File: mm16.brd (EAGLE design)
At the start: 100 x 80 mm, 57 parts, among them IC101 ATMEGA32-PU, IC102 DS1337, IC103 MAX483CPA, IC201 LTV847, IC202 LTV847, IC203 LTV847, IC204 LTV847, Q1 32,768kHz

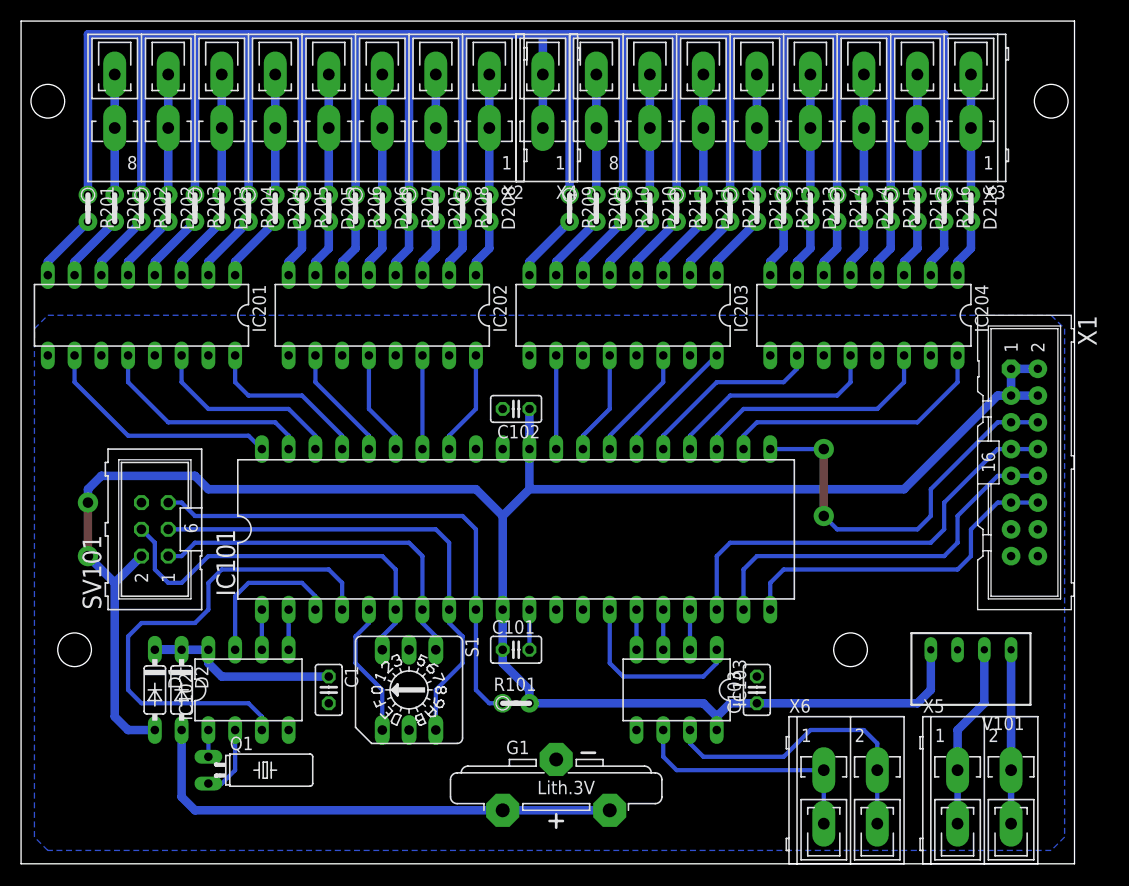
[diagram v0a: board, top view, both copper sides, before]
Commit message: Anschlussklemmen ausgetauscht
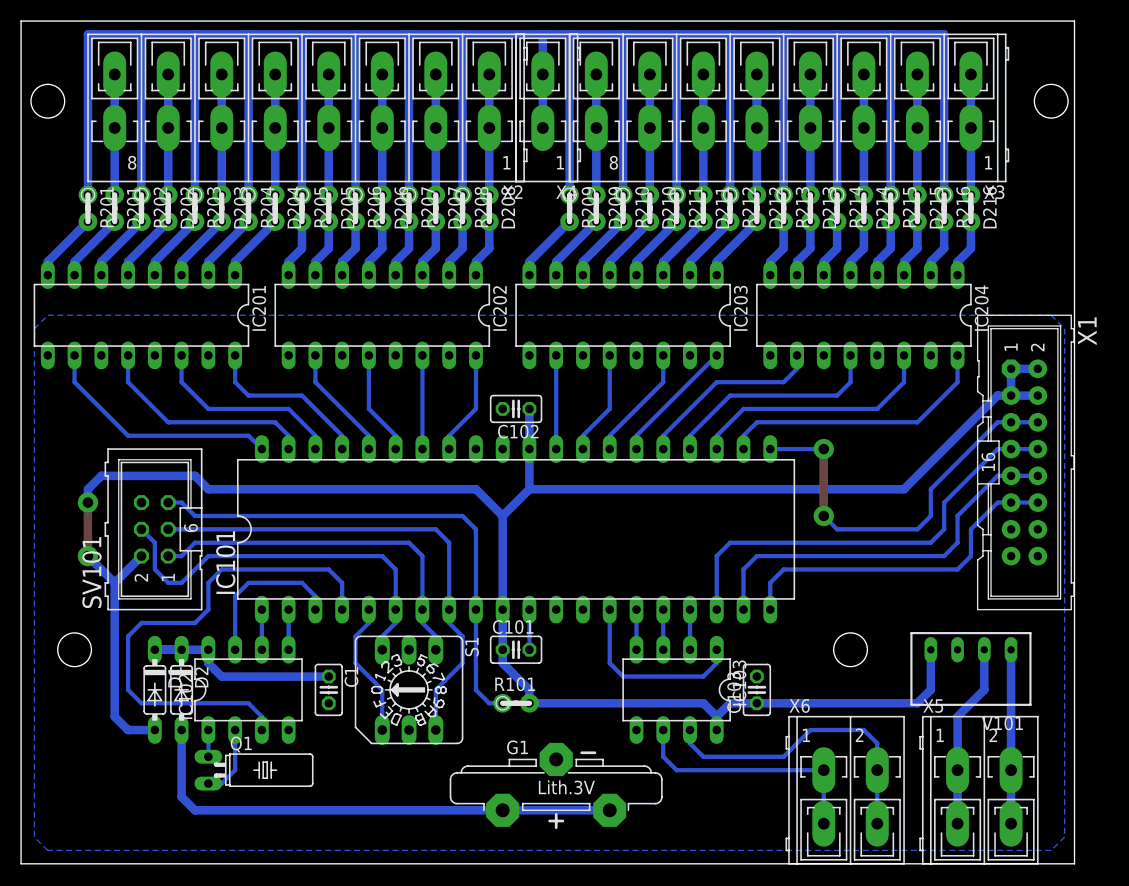
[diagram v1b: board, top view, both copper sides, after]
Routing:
- net N$83: track 11.4 -> 16.5 mm

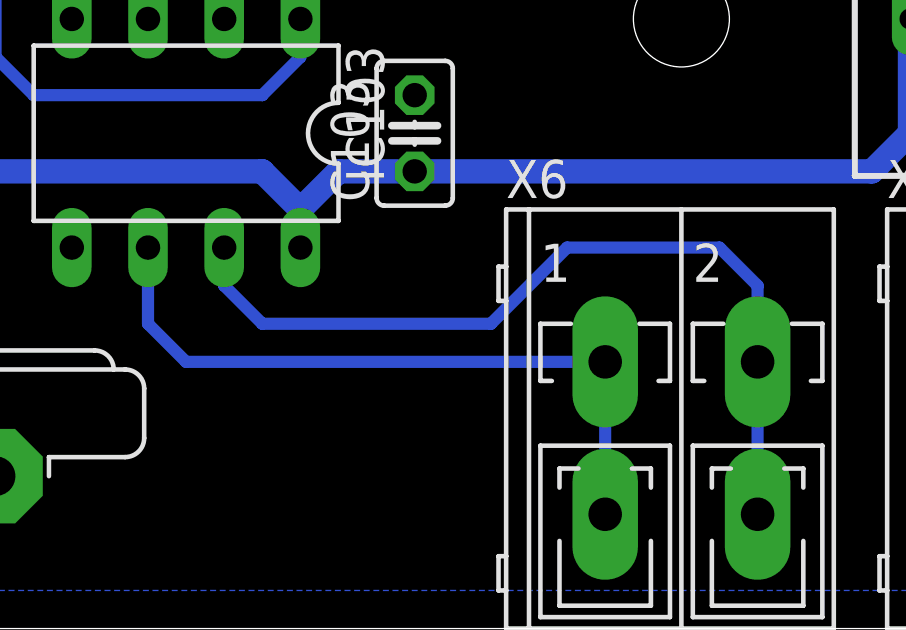
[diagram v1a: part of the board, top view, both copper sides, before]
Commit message: Optionaler Abschlusswiderstand eingefügt
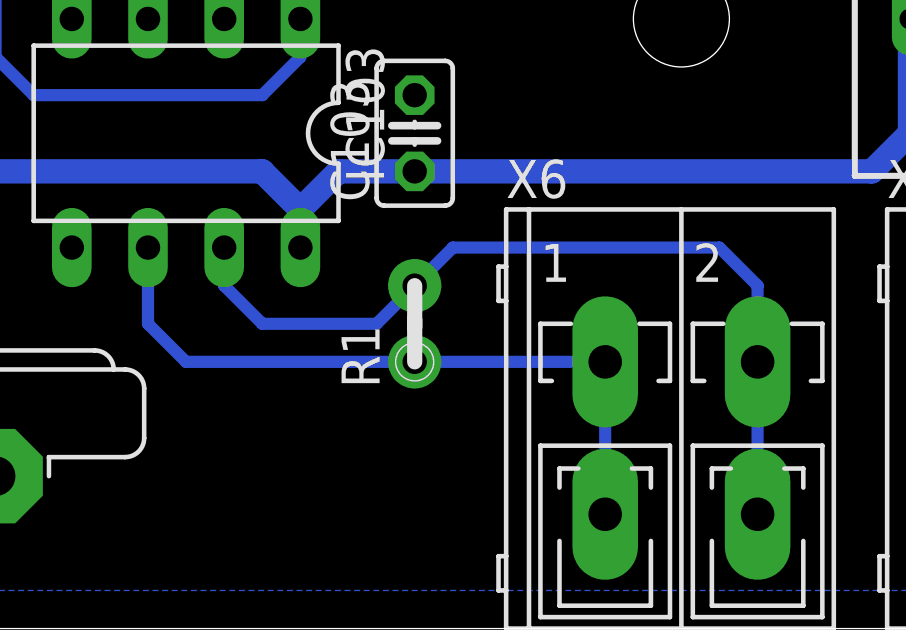
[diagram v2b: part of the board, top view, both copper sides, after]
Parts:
- added R1: 120Ω, passiv:0204V
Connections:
- removed net N$19: IC103.7, X6.A2, X6.B2
- new net N$22: IC103.7, R1.2, X6.A2, X6.B2
- net N$20: now also R1.1
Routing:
- net N$19: track 28.8 -> 0.00 mm
- net N$22: track 0.00 -> 28.8 mm
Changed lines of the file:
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@@
 <element name="X2" library="anschluss" package="WAGO_236-408" value="" x="26.67" y="71.12" rot="R180"/>
 <element name="X3" library="anschluss" package="WAGO_236-408" value="" x="72.39" y="71.12" rot="R180"/>
+<element name="R1" library="passiv" package="0204V" value="120Ω" x="69.85" y="10.16" rot="R90"/>
 </elements>
 <signals>
@@
 <wire x1="49.53" y1="74.93" x2="49.53" y2="78.74" width="0.8128" layer="16"/>
 </signal>
-<signal name="N$19">
-<contactref element="IC103" pad="7"/>
-<wire x1="63.5" y1="12.7" x2="63.5" y2="11.43" width="0.4064" layer="16"/>
-<wire x1="63.5" y1="11.43" x2="64.77" y2="10.16" width="0.4064" layer="16"/>
-<wire x1="64.77" y1="10.16" x2="72.39" y2="10.16" width="0.4064" layer="16"/>
-<wire x1="72.39" y1="10.16" x2="74.93" y2="12.7" width="0.4064" layer="16"/>
-<wire x1="74.93" y1="12.7" x2="80.01" y2="12.7" width="0.4064" layer="16"/>
-<wire x1="80.01" y1="12.7" x2="81.28" y2="11.43" width="0.4064" layer="16"/>
-<contactref element="X6" pad="B2" route="any" routetag="A"/>
-<contactref element="X6" pad="A2" route="any" routetag="A"/>
-<wire x1="81.28" y1="8.89" x2="81.28" y2="11.43" width="0.4064" layer="16"/>
-<wire x1="81.28" y1="8.89" x2="81.28" y2="3.81" width="0.4064" layer="16"/>
-</signal>
 <signal name="N$20">
 <contactref element="IC103" pad="6"/>
+<contactref element="X6" pad="A1" route="any" routetag="A"/>
+<contactref element="X6" pad="B1" route="any" routetag="A"/>
+<wire x1="76.2" y1="8.89" x2="76.2" y2="3.81" width="0.4064" layer="16"/>
+<contactref element="R1" pad="1"/>
 <wire x1="60.96" y1="12.7" x2="60.96" y2="10.16" width="0.4064" layer="16"/>
 <wire x1="60.96" y1="10.16" x2="62.23" y2="8.89" width="0.4064" layer="16"/>
-<contactref element="X6" pad="A1" route="any" routetag="A"/>
-<contactref element="X6" pad="B1" route="any" routetag="A"/>
-<wire x1="76.2" y1="8.89" x2="62.23" y2="8.89" width="0.4064" layer="16"/>
-<wire x1="76.2" y1="8.89" x2="76.2" y2="3.81" width="0.4064" layer="16"/>
+<wire x1="62.23" y1="8.89" x2="69.85" y2="8.89" width="0.4064" layer="16"/>
+<wire x1="69.85" y1="8.89" x2="76.2" y2="8.89" width="0.4064" layer="16"/>
 </signal>
 <signal name="VCC">
@@
 <wire x1="93.98" y1="8.89" x2="93.98" y2="3.81" width="0.8128" layer="16"/>
 </signal>
+<signal name="N$22">
+<contactref element="R1" pad="2"/>
+<contactref element="IC103" pad="7"/>
+<contactref element="X6" pad="B2" route="any" routetag="A"/>
+<contactref element="X6" pad="A2" route="any" routetag="A"/>
+<wire x1="63.5" y1="12.7" x2="63.5" y2="11.43" width="0.4064" layer="16"/>
+<wire x1="63.5" y1="11.43" x2="64.77" y2="10.16" width="0.4064" layer="16"/>
+<wire x1="80.01" y1="12.7" x2="81.28" y2="11.43" width="0.4064" layer="16"/>
+<wire x1="81.28" y1="8.89" x2="81.28" y2="11.43" width="0.4064" layer="16"/>
+<wire x1="81.28" y1="8.89" x2="81.28" y2="3.81" width="0.4064" layer="16"/>
+<wire x1="64.77" y1="10.16" x2="68.58" y2="10.16" width="0.4064" layer="16"/>
+<wire x1="68.58" y1="10.16" x2="69.85" y2="11.43" width="0.4064" layer="16"/>
+<wire x1="69.85" y1="11.43" x2="71.12" y2="12.7" width="0.4064" layer="16"/>
+<wire x1="71.12" y1="12.7" x2="80.01" y2="12.7" width="0.4064" layer="16"/>
+</signal>
 </signals>

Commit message: Batteriehalter ausgetauscht
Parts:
- G1: value CR2032V -> KZH20PCB-V; device battery:CR2032V -> batterie:KZH20PCB-V
- moved G1 1.80 mm to (49.5, 6.35), turned to 180 degrees
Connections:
- net N$21: now also G1.+1, G1.+2; no longer G1.+, G1.+@1
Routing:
- net N$21: track 47.5 -> 36.1 mm
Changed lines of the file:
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@@
 </classes>
 <designrules>
-<description language="de">&lt;b&gt;EAGLE Design Rules&lt;/b&gt;
-&lt;p&gt;
-Die Standard-Design-Rules sind so gewählt, dass sie für
-die meisten Anwendungen passen. Sollte ihre Platine
-besondere Anforderungen haben, treffen Sie die erforderlichen
-Einstellungen hier und speichern die Design Rules unter
-einem neuen Namen ab.</description>
-<description language="en">&lt;b&gt;EAGLE Design Rules&lt;/b&gt;
+<description language="de">
+&lt;b&gt;Standardwerte für Eigenbau&lt;/b&gt;
+</description>
+<description language="en">
+&lt;b&gt;EAGLE Design Rules&lt;/b&gt;
 &lt;p&gt;
 The default Design Rules have been set to cover
@@
 <param name="mtCopper" value="0.035mm 0.035mm 0.035mm 0.035mm 0.035mm 0.035mm 0.035mm 0.035mm 0.035mm 0.035mm 0.035mm 0.035mm 0.035mm 0.035mm 0.035mm 0.035mm"/>
 <param name="mtIsolate" value="1.5mm 0.15mm 0.2mm 0.15mm 0.2mm 0.15mm 0.2mm 0.15mm 0.2mm 0.15mm 0.2mm 0.15mm 0.2mm 0.15mm 0.2mm"/>
-<param name="mdWireWire" value="8mil"/>
-<param name="mdWirePad" value="8mil"/>
-<param name="mdWireVia" value="8mil"/>
-<param name="mdPadPad" value="8mil"/>
-<param name="mdPadVia" value="8mil"/>
-<param name="mdViaVia" value="8mil"/>
-<param name="mdSmdPad" value="8mil"/>
-<param name="mdSmdVia" value="8mil"/>
-<param name="mdSmdSmd" value="8mil"/>
+<param name="mdWireWire" value="16mil"/>
+<param name="mdWirePad" value="16mil"/>
+<param name="mdWireVia" value="16mil"/>
+<param name="mdPadPad" value="16mil"/>
+<param name="mdPadVia" value="16mil"/>
+<param name="mdViaVia" value="16mil"/>
+<param name="mdSmdPad" value="16mil"/>
+<param name="mdSmdVia" value="16mil"/>
+<param name="mdSmdSmd" value="16mil"/>
 <param name="mdViaViaSameLayer" value="8mil"/>
 <param name="mnLayersViaInSmd" value="2"/>
-<param name="mdCopperDimension" value="40mil"/>
-<param name="mdDrill" value="8mil"/>
+<param name="mdCopperDimension" value="1mm"/>
+<param name="mdDrill" value="1mm"/>
 <param name="mdSmdStop" value="0mil"/>
-<param name="msWidth" value="10mil"/>
-<param name="msDrill" value="24mil"/>
+<param name="msWidth" value="16mil"/>
+<param name="msDrill" value="0.6mm"/>
 <param name="msMicroVia" value="9.99mm"/>
 <param name="msBlindViaRatio" value="0.5"/>
@@
 <param name="dpMaxLengthDifference" value="10mm"/>
 <param name="dpGapFactor" value="2.5"/>
-<param name="checkGrid" value="0"/>
-<param name="checkAngle" value="0"/>
+<param name="checkGrid" value="1"/>
+<param name="checkAngle" value="1"/>
 <param name="checkFont" value="1"/>
 <param name="checkRestrict" value="1"/>
@@
 <element name="D1" library="diode" package="DO35-7" value="1N4148-7" x="12.7" y="16.51" rot="R270"/>
 <element name="D2" library="diode" package="DO35-7" value="1N4148-7" x="15.24" y="16.51" rot="R270"/>
-<element name="G1" library="battery" package="CR2032V" value="CR2032V" x="50.8" y="7.62" rot="R90"/>
 <element name="S1" library="switch-dil" package="P103" value="" x="36.83" y="16.51" rot="R270">
 <attribute name="OC_NEWARK" value="unknown" x="36.83" y="16.51" size="1.778" layer="27" rot="R270" display="off"/>
@@
 <element name="X3" library="anschluss" package="WAGO_236-408" value="" x="72.39" y="71.12" rot="R180"/>
 <element name="R1" library="passiv" package="0204V" value="120Ω" x="69.85" y="10.16" rot="R90"/>
+<element name="G1" library="batterie" package="KZH20PCB-V" value="KZH20PCB-V" x="49.53" y="6.35" rot="R180"/>
 </elements>
 <signals>
@@
 </polygon>
 <contactref element="IC201" pad="9"/>
+<contactref element="S1" pad="C"/>
 <contactref element="G1" pad="-"/>
-<contactref element="S1" pad="C"/>
 </signal>
 <signal name="IN0">
@@
 <signal name="N$21">
 <contactref element="D2" pad="A"/>
-<contactref element="G1" pad="+"/>
-<contactref element="G1" pad="+@1"/>
-<wire x1="55.88" y1="5.08" x2="45.72" y2="5.08" width="0.8128" layer="16"/>
 <wire x1="15.24" y1="12.7" x2="15.24" y2="6.35" width="0.8128" layer="16"/>
 <wire x1="15.24" y1="6.35" x2="16.51" y2="5.08" width="0.8128" layer="16"/>
-<wire x1="16.51" y1="5.08" x2="45.72" y2="5.08" width="0.8128" layer="16"/>
+<contactref element="G1" pad="+2" route="any" routetag="+"/>
+<contactref element="G1" pad="+1" route="any" routetag="+"/>
+<wire x1="16.51" y1="5.08" x2="44.45" y2="5.08" width="0.8128" layer="16"/>
 </signal>
 <signal name="ALARM1">
